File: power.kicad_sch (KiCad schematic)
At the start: 31 parts, among them SW1 SW_Push, U2 BQ25180YBGR, U3 TPS63802DLAR, U4 LP5907MFX-3.3/NOPB, U5 LM27762DSSR, U6 MAX17048G+T10

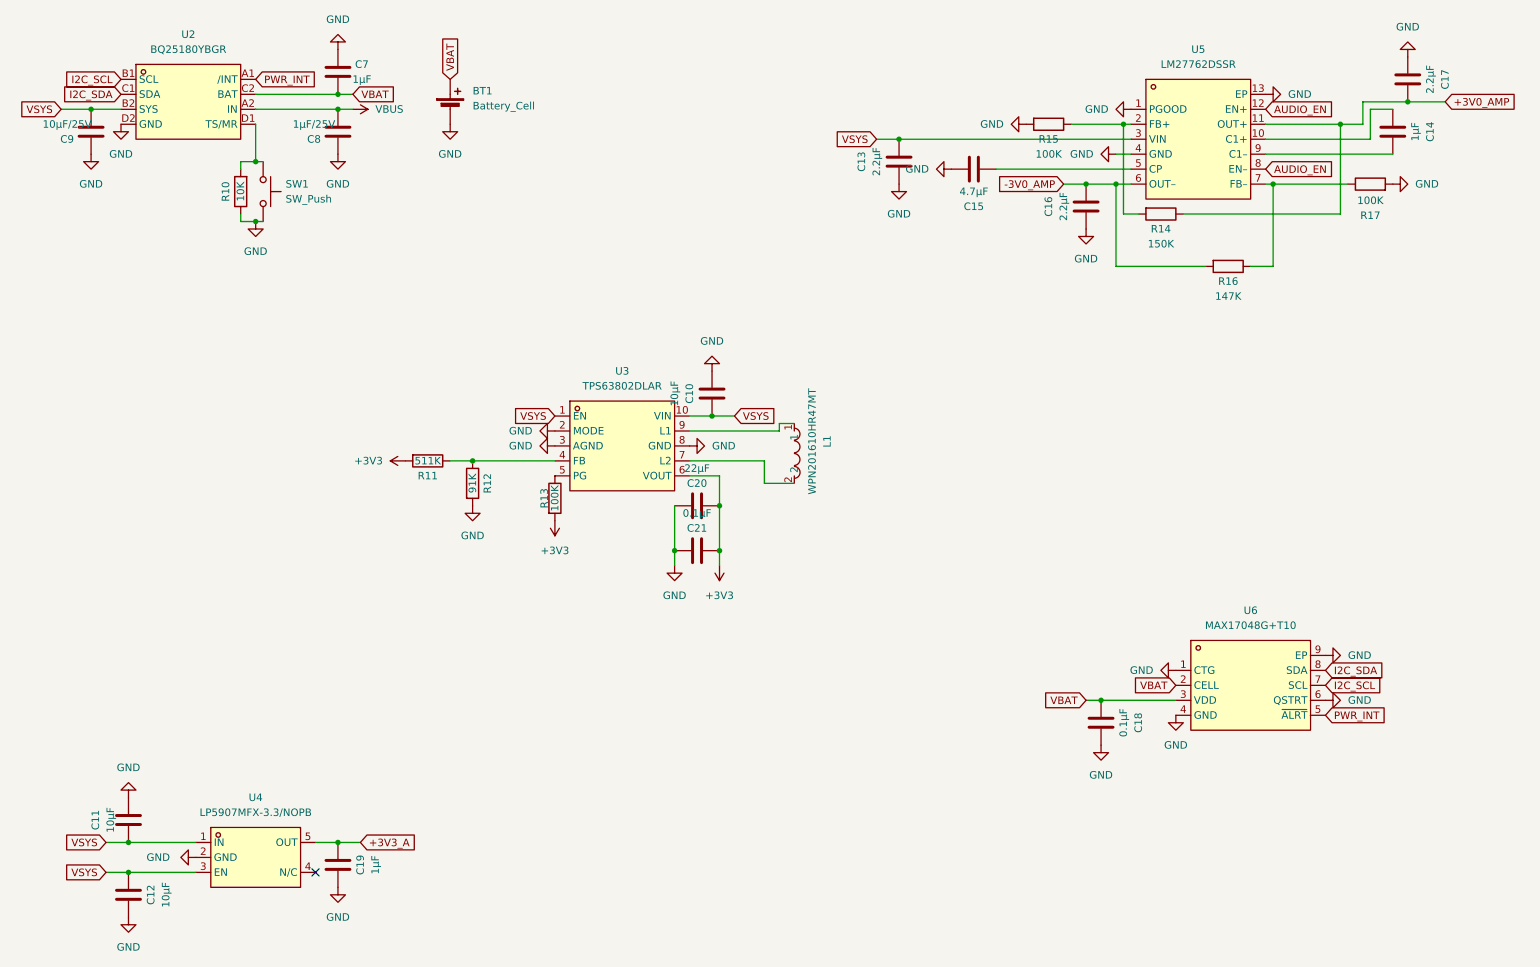
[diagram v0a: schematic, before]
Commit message: Schematic done
- sheet files renamed to English (usb, power, esp32, audio, io)
- final layout, annotation R1-R42 / C1-C43 / U1-U9 / J1-J4 / SW1-SW8
- all buttons are TS-1088, project R/C symbols, PWR_FLAGs
- connections.md replaces conexiuni.md (English, final references)
- final check on the KiCad netlist: 278/278 checks against connections.md
- status updated; firmware note: BQ25180 charge current defaults to ~10 mA

Co-Authored-By: Claude Opus 5.5 <noreply@anthropic.com>
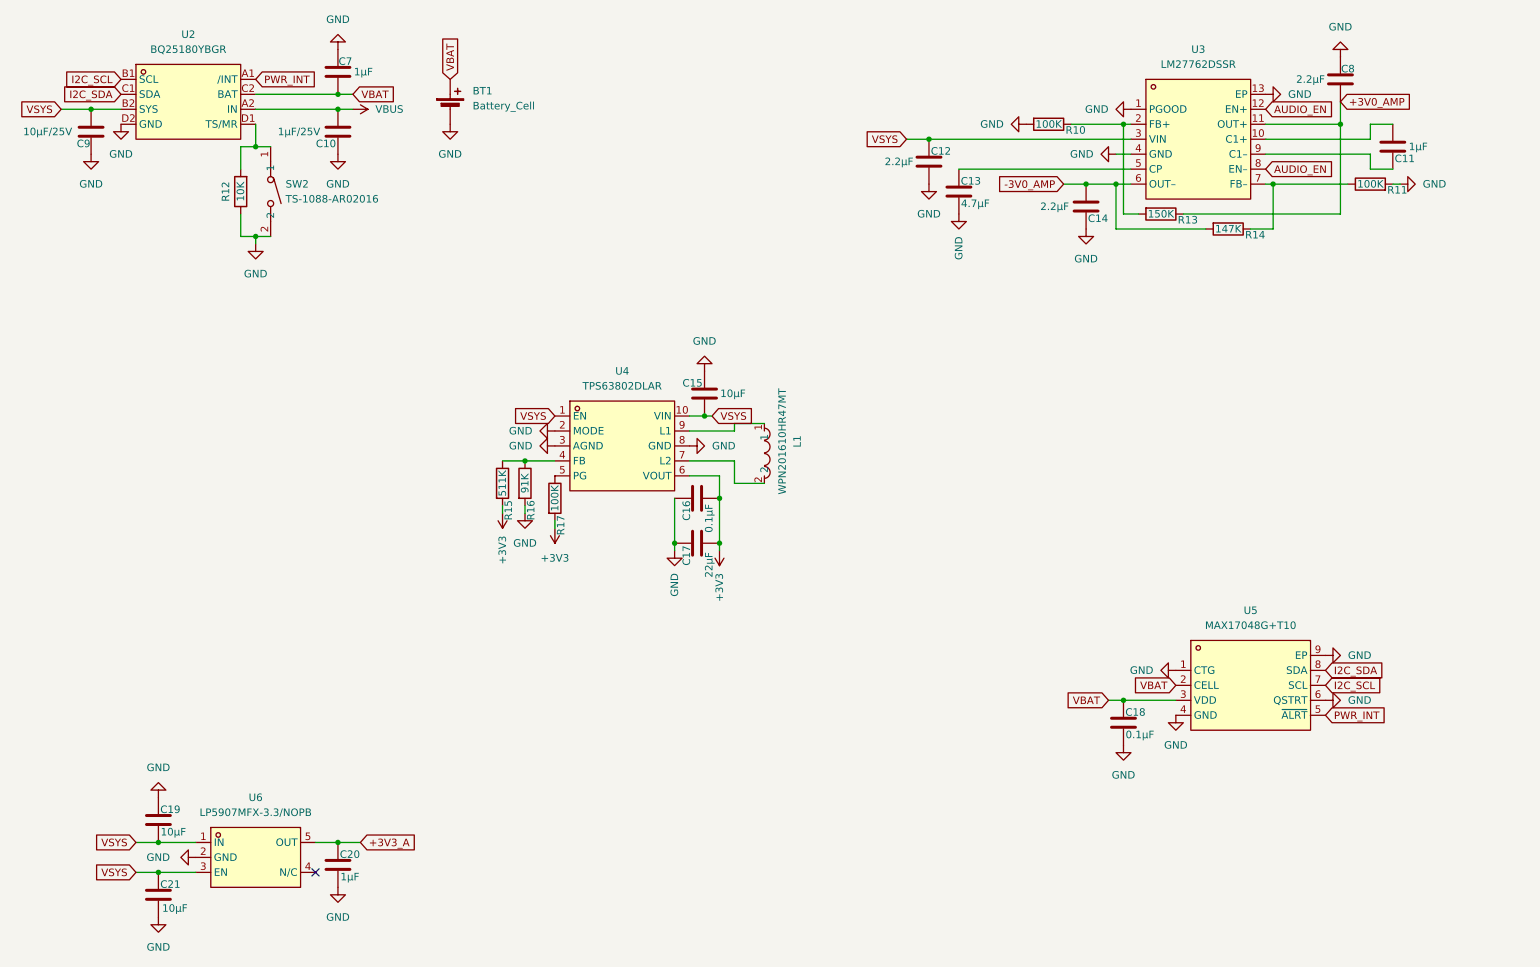
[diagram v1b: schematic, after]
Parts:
- removed C20: 22µF, symbol Device:C
- removed C21: 0.1µF, symbol Device:C
- removed SW1: SW_Push, symbol Switch:SW_Push
- added C16: 0.1µF, symbol Device:C
- added C17: 22µF, symbol Device:C
- added SW2: TS-1088-AR02016, mp3_player:SW-SMD_L3.9-W3.0-P4.45, symbol mp3_player:TS-1088-AR02016
- R10: renamed from R15; symbol Device:R -> mp3_player:R
- R11: renamed from R17; symbol Device:R -> mp3_player:R
- R12: renamed from R10; symbol Device:R -> mp3_player:R
- R13: renamed from R14; symbol Device:R -> mp3_player:R
- R14: renamed from R16; symbol Device:R -> mp3_player:R
- R15: renamed from R11; symbol Device:R -> mp3_player:R
- R16: renamed from R12; symbol Device:R -> mp3_player:R
- R17: renamed from R13; symbol Device:R -> mp3_player:R
- renumbered C8 to C10, C14 to C11, C13 to C12, C15 to C13, C16 to C14, C10 to C15, C11 to C19, C19 to C20, C12 to C21, C17 to C8, U5 to U3, U3 to U4, U6 to U5, U4 to U6
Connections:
- net +3V3: now also C16.1, C17.1
- net GND: now also C16.2, C17.2, SW2.2
- net at R12.2, U2.D1 (TS/MR): now also SW2.1
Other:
- moved on the sheet: C11, C12, C13, C15, C18, C19, C21, C8, L1, R14, R15, R16

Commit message: Assign footprints and LCSC parts to passives, D2 and BT1
Thin-film 0.1% resistors in the audio path and rail dividers, C0G caps
in the DAC output filter, Samsung/Murata MLCCs with 0603/0805 cases for
bulk caps. Passive choices documented in mp3_player.md.

Co-Authored-By: Claude Opus 5.5 <noreply@anthropic.com>
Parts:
- BT1: footprint (none) -> Connector_JST:JST_PH_S2B-PH-SM4-TB_1x02-1MP_P2.00mm_Horizontal; LCSC Part (none) -> C295747
- C10: footprint (none) -> Capacitor_SMD:C_0603_1608Metric; LCSC Part (none) -> C15849
- C11, C20, C7: footprint (none) -> Capacitor_SMD:C_0402_1005Metric; LCSC Part (none) -> C52923
- C12, C14, C8: footprint (none) -> Capacitor_SMD:C_0603_1608Metric; LCSC Part (none) -> C23630
- C13: footprint (none) -> Capacitor_SMD:C_0603_1608Metric; LCSC Part (none) -> C19666
- C15, C19, C21: footprint (none) -> Capacitor_SMD:C_0603_1608Metric; LCSC Part (none) -> C96446
- C16, C18: footprint (none) -> Capacitor_SMD:C_0402_1005Metric; LCSC Part (none) -> C1525
- C17: footprint (none) -> Capacitor_SMD:C_0805_2012Metric; LCSC Part (none) -> C45783
- C9: footprint (none) -> Capacitor_SMD:C_0805_2012Metric; LCSC Part (none) -> C15850
- R10, R11, R17: footprint (none) -> Resistor_SMD:R_0402_1005Metric; LCSC Part (none) -> C852472
- R12: footprint (none) -> Resistor_SMD:R_0402_1005Metric; LCSC Part (none) -> C190095
- R13: footprint (none) -> Resistor_SMD:R_0402_1005Metric; LCSC Part (none) -> C852538
- R14: footprint (none) -> Resistor_SMD:R_0402_1005Metric; LCSC Part (none) -> C5197520
- R15: footprint (none) -> Resistor_SMD:R_0402_1005Metric; LCSC Part (none) -> C163461
- R16: footprint (none) -> Resistor_SMD:R_0402_1005Metric; LCSC Part (none) -> C852952

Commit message: BT1: JST PH footprint with 3D model from LCSC
KiCad's stock S2B-PH-SM4-TB footprint has no 3D model, so use the
EasyEDA one (C295747) like the other custom parts.

Co-Authored-By: Claude Opus 5.5 <noreply@anthropic.com>
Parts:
- BT1: footprint Connector_JST:JST_PH_S2B-PH-SM4-TB_1x02-1MP_P2.00mm_Horizontal -> mp3_player:CONN-SMD_P2.00_S2B-PH-SM4-TB-LF-SN
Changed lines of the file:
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@@
 			)
 		)
-		(property "Footprint" "Connector_JST:JST_PH_S2B-PH-SM4-TB_1x02-1MP_P2.00mm_Horizontal"
+		(property "Footprint" "mp3_player:CONN-SMD_P2.00_S2B-PH-SM4-TB-LF-SN"
 			(at 99.06 35.306 90)
 			(hide yes)

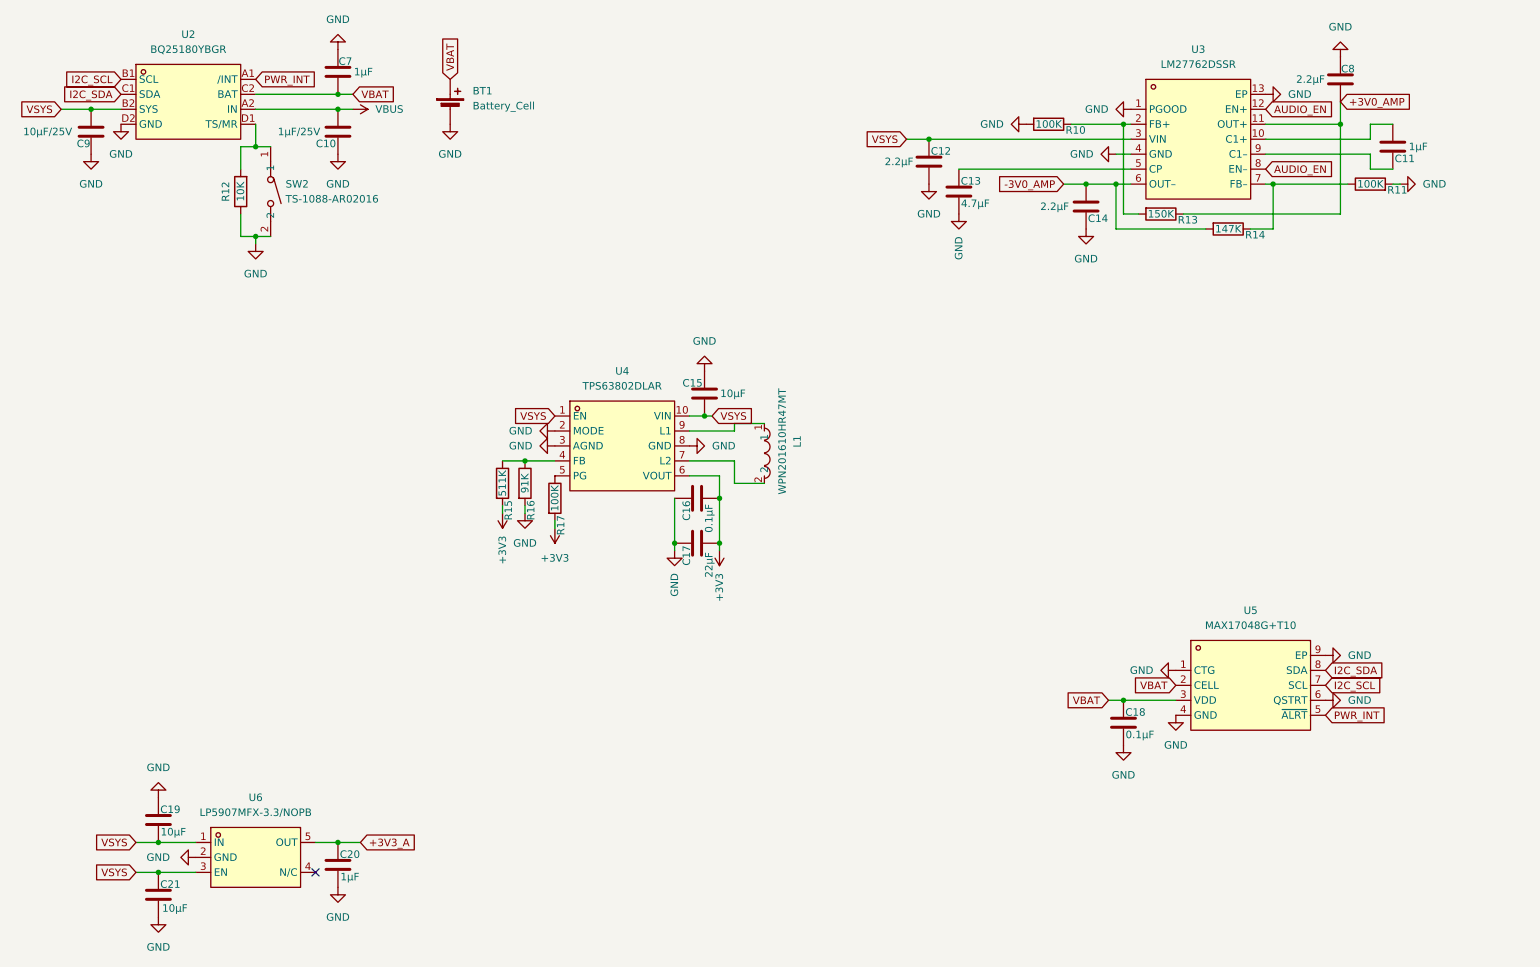
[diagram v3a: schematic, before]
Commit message: Fix ERC and document enclosure concept
- ERC clean: power flags moved onto real nets, USBLC6 pin types,
  Unspecified pins allowed in the pin conflict map, off-grid wires aligned
- mp3_player.md: enclosure section (anodized aluminium v1, titanium v2,
  printed click wheel and antenna cap, build123d workflow)
- ignore the build123d venv

Co-Authored-By: Claude Opus 5.5 <noreply@anthropic.com>
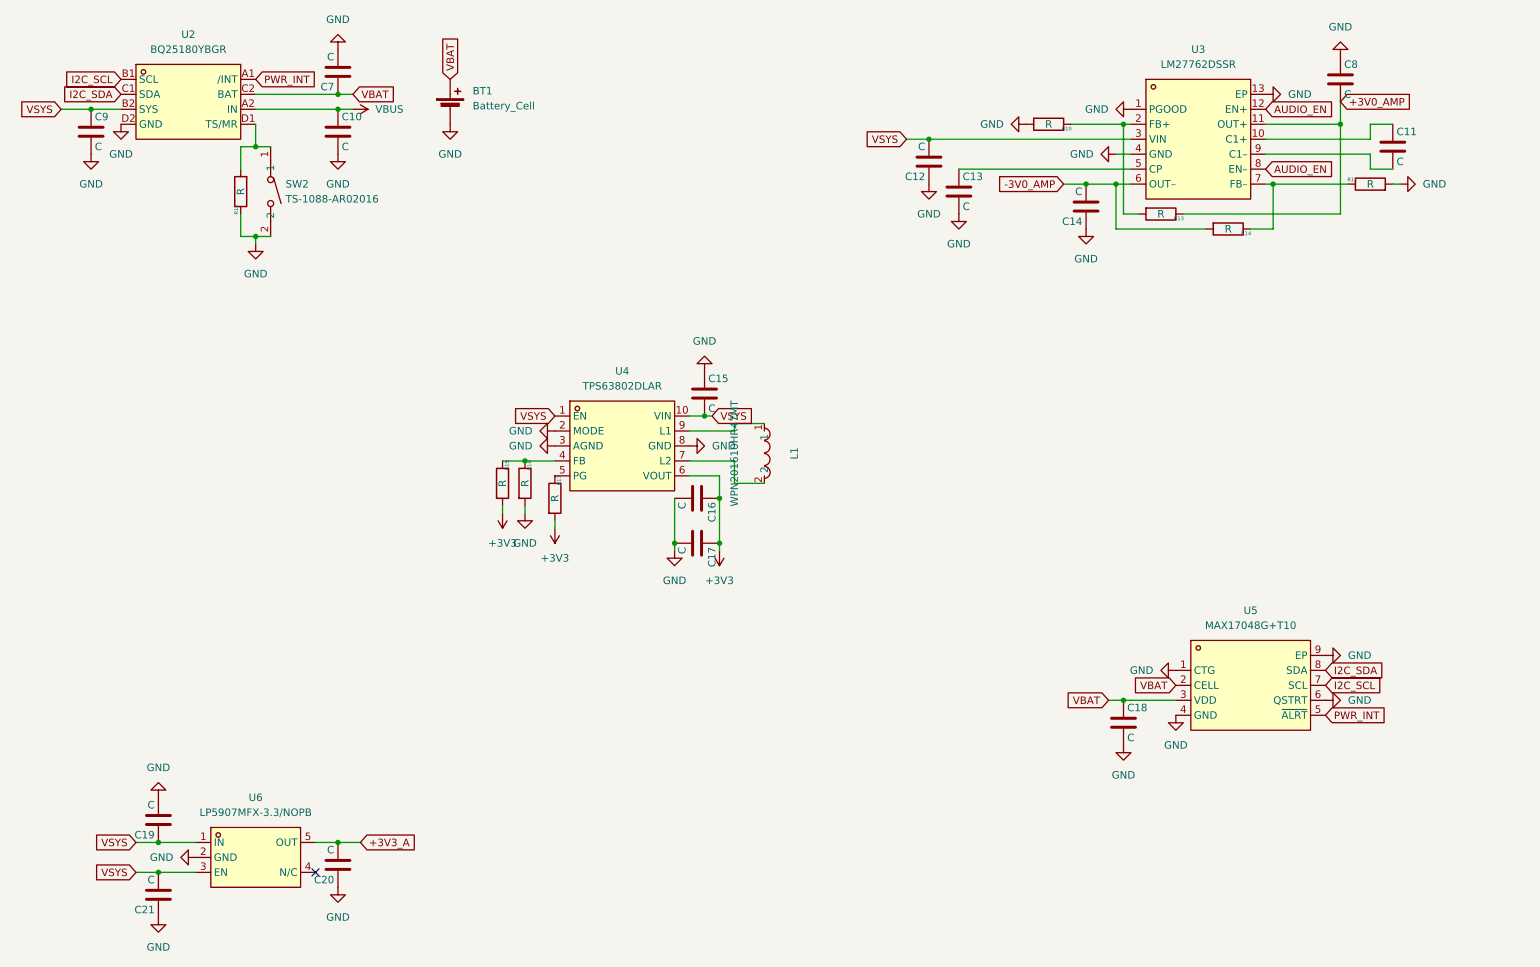
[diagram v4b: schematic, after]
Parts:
- C10: value 1µF/25V -> C
- C11, C20, C7: value 1µF -> C
- C12, C14, C8: value 2.2µF -> C
- C13: value 4.7µF -> C
- C15, C19, C21: value 10µF -> C
- C16, C18: value 0.1µF -> C
- C17: value 22µF -> C
- C9: value 10µF/25V -> C
- R10, R11, R17: value 100K -> R
- R12: value 10K -> R
- R13: value 150K -> R
- R14: value 147K -> R
- R15: value 511K -> R
- R16: value 91K -> R

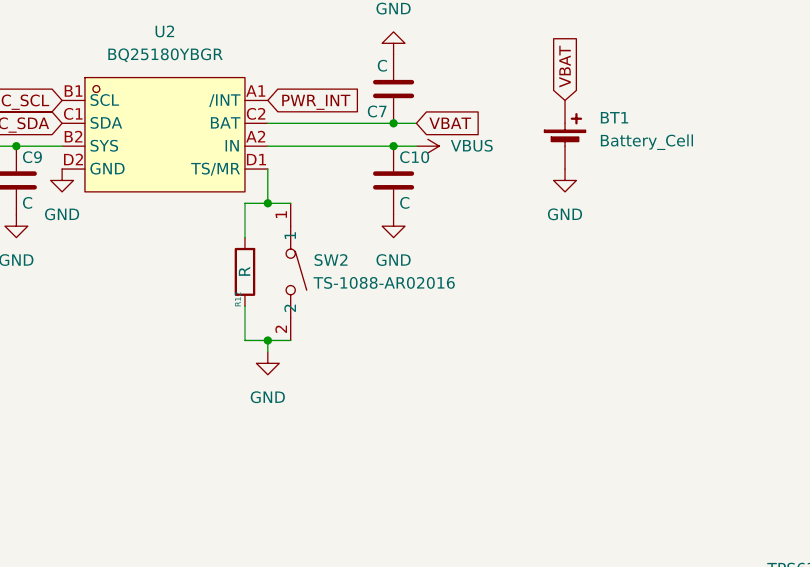
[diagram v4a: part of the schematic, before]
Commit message: Schematic and parts for enclosure B
- jack PJ-342C CB (TRRS, sinking) as CN1, HP-DET on JACK_SW, MIC to GND,
  100nF on JACK_DET (detect is now active low)
- USB-C TYPE-C 16P CB0.8 073 (sinking, 0.8 mm board) as USB1
- BT1 on JST SH SM02B-SRSS-TB, click wheel on TS-1187B-B (0.75 mm),
  power on EVQP7J01P side switch
- new footprints/3D models in lib; switch and JST SH footprints renumbered
  so the existing 2-pin symbols fit
- enclosure: power key on the right side, level with the display
- docs: connections.md, code.md and BOM updated

ERC: 0 errors, 0 warnings.

Co-Authored-By: Claude Opus 5.5 <noreply@anthropic.com>
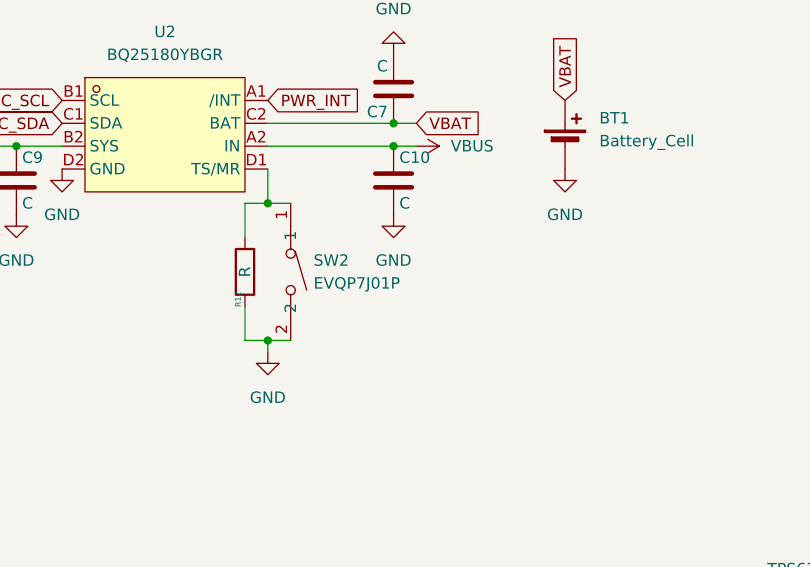
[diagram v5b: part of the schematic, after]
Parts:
- BT1: footprint mp3_player:CONN-SMD_P2.00_S2B-PH-SM4-TB-LF-SN -> mp3_player:CONN-SMD_2P-P1.00_SM02B-SRSS-TB-LF-SN; LCSC Part C295747 -> C160402
- SW2: value TS-1088-AR02016 -> EVQP7J01P; footprint mp3_player:SW-SMD_L3.9-W3.0-P4.45 -> mp3_player:SW-SMD_EVQP7J01P; LCSC Part C720477 -> C2828254
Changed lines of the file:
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@@
 			)
 		)
-		(property "Value" "TS-1088-AR02016"
+		(property "Value" "EVQP7J01P"
 			(at 71.12 52.0699 90)
 			(show_name no)
@@
 			)
 		)
-		(property "Footprint" "mp3_player:SW-SMD_L3.9-W3.0-P4.45"
+		(property "Footprint" "mp3_player:SW-SMD_EVQP7J01P"
 			(at 60.96 50.8 0)
 			(hide yes)
@@
 			)
 		)
-		(property "LCSC Part" "C720477"
+		(property "LCSC Part" "C2828254"
 			(at 50.8 50.8 0)
 			(hide yes)
@@
 			)
 		)
-		(property "Footprint" "mp3_player:CONN-SMD_P2.00_S2B-PH-SM4-TB-LF-SN"
+		(property "Footprint" "mp3_player:CONN-SMD_2P-P1.00_SM02B-SRSS-TB-LF-SN"
 			(at 99.06 35.306 90)
 			(hide yes)
@@
 			)
 		)
-		(property "LCSC Part" "C295747"
+		(property "LCSC Part" "C160402"
 			(at 99.06 35.306 90)
 			(hide yes)
